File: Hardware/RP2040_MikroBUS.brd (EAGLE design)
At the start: 30.5 x 94 mm, 144 parts, among them J1 SWD, J3 Qwiic, J5 USB C, J6 microSD, Q1 20V/4.2A/52mΩ/1.4W, U2 MAX17048, U3 MCP73831, U4 W25QXX128MBIT, U5 RP2040, U6 WS2812-2020, U7 3.3V, Y2 12MHz

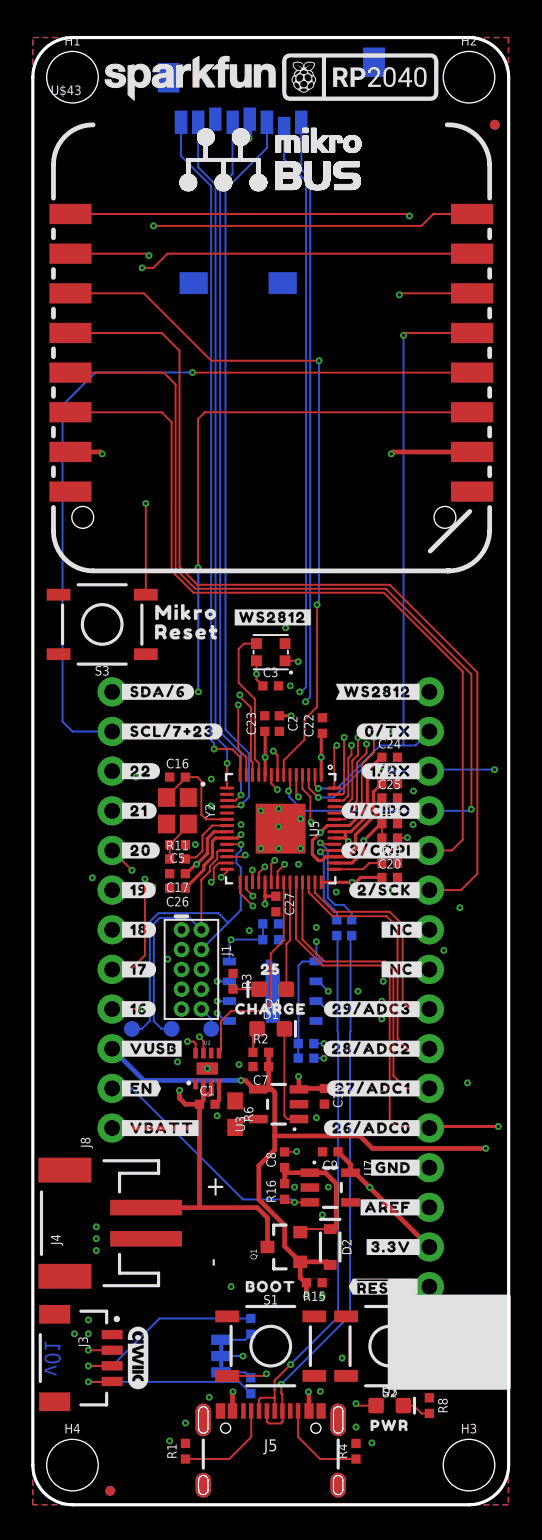
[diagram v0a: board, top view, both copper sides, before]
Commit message: Schematic updates
* Remove values from TPs
* Updated net labels with "!" for active low signals - !BOOT!, !SPI0_CS!, !QSPI-CS!, !BATT_ALERT!
* Updated name, value, and shape of mikroBUS socket sch symbol
* Switched out SD card socket for the new one, did NOT connect the detect pin
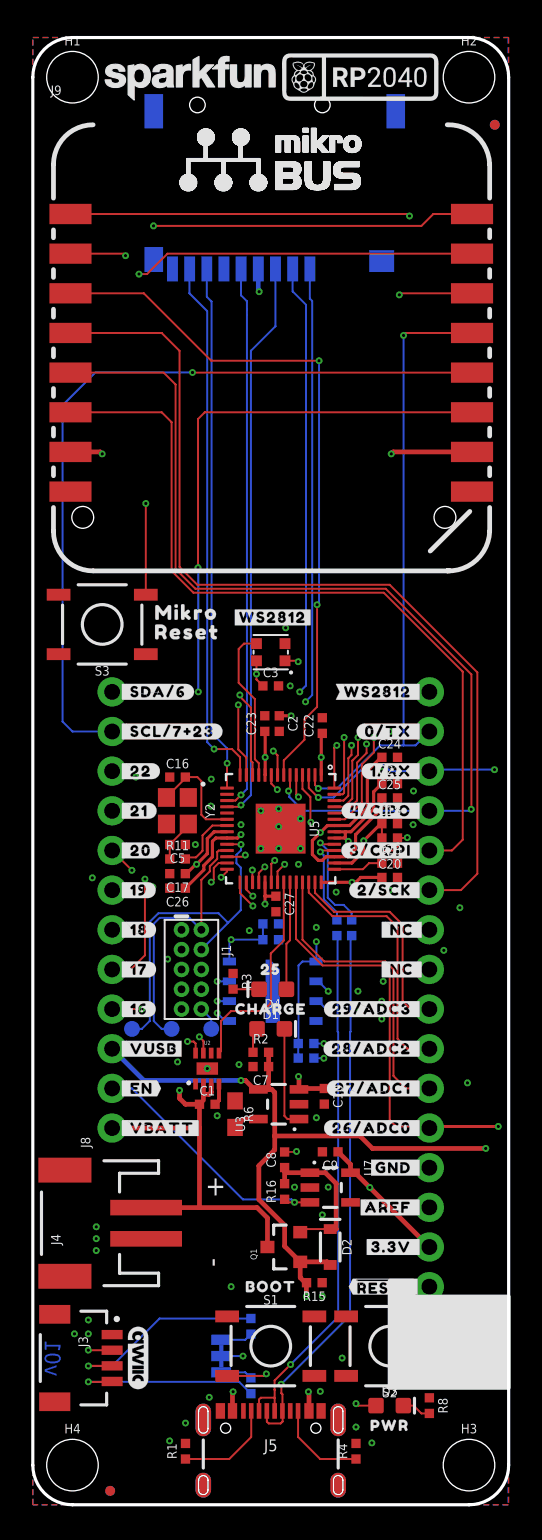
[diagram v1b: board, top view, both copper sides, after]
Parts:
- J6: device SparkFun-Connectors:MICRO-SD-SOCKET -> SparkFun-Connectors:MICROSD-EXTERNALPIN
- moved J6 13.9 mm to (15.5, 89.7), turned to 180 degrees
- renumbered U$43 to J9
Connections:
- net BATT_ALERT renamed !BATT_ALERT!
- net BOOT renamed !BOOT!
- net QSPI-CS renamed !QSPI-CS!
- net SPI0_CS renamed !SPI0_CS!
- net 3.3V: now also J6.4; no longer J6.VCC
- net GND: now also J6.10, J6.11, J6.12, J6.13, J6.6, J6.9; no longer J6.CD1, J6.GND, J6.GND1, J6.GND3
- net SDIO_DAT1: now also J6.8; no longer J6.DAT1
- net SDIO_DAT2: now also J6.1; no longer J6.DAT2
- net SPI_!CS1!/SDIO_DAT3: now also J6.2; no longer J6.CS/DAT3
- net SPI_CIPO1/SDIO_DAT0: now also J6.7; no longer J6.DO/DAT0
- net SPI_COPI1/SDIO_CMD: now also J6.3; no longer J6.DI/CMD
- net SPI_SCK1/SDIO_CLK: now also J6.5; no longer J6.SCLK
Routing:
- net SPI_COPI1/SDIO_CMD: track 46.6 -> 36.2 mm
- net SPI_SCK1/SDIO_CLK: track 45.0 -> 35.1 mm
- net SPI_CIPO1/SDIO_DAT0: track 43.4 -> 33.8 mm
- net SDIO_DAT1: track 44.0 -> 34.4 mm
- net SDIO_DAT2: track 46.6 -> 37.1 mm
- net SPI_!CS1!/SDIO_DAT3: track 46.3 -> 37.0 mm
- net MIK_RST: track 26.9 -> 26.3 mm

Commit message: Board updates
* Fix RESET button label
* Add RP2040 to SF microcontroller library and update in sch/board
* Gave some more space between the new traces I placed
* Brought D+ and D- traces closer together
* Changed "WS2812" label to text only
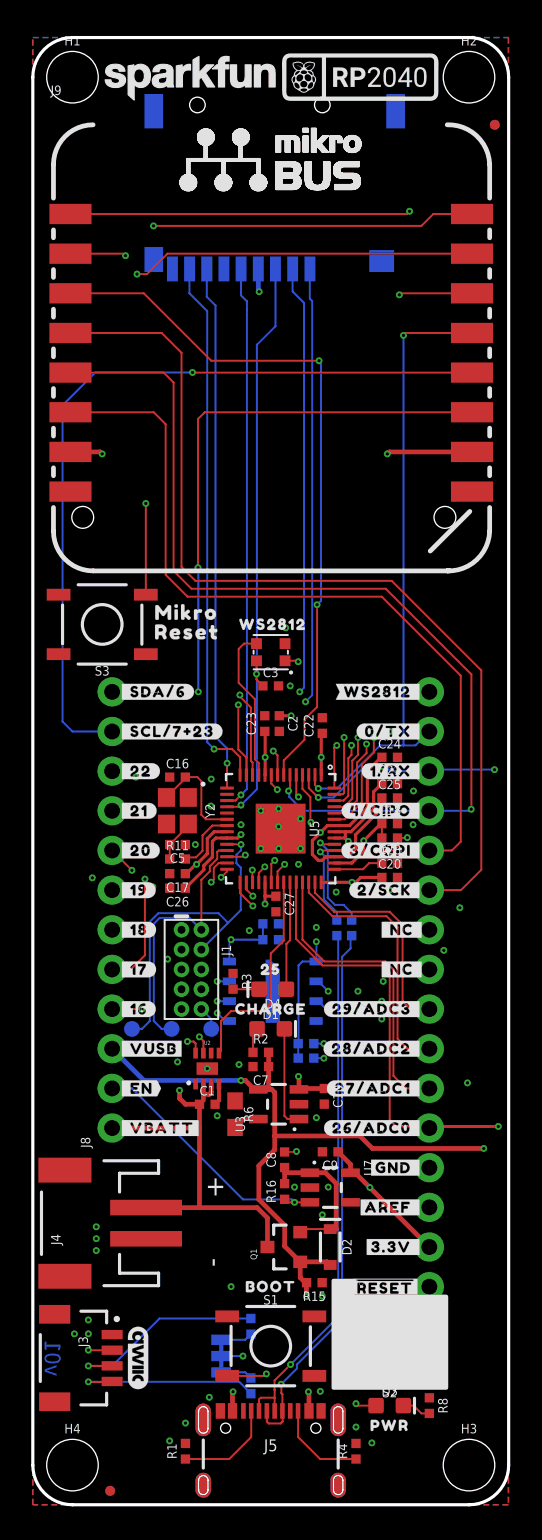
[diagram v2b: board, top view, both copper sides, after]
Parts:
- removed U$60: (no value), output:#WS2812#0
- added U$30: (no value), output:WS28120
- U5: device RP2040:QFN-56 -> SparkFun-IC-Microcontroller:QFN-56
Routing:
- net I2C1_SCL/GPIO23: track 140.4 -> 139.2 mm

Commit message: Run checklist
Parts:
- removed U$45: (no value), SparkFun-Aesthetics:SFE_LOGO_NAME_.1
- added LOGO1: OSHW-LOGOS, SparkFun-Aesthetics:OSHW-LOGO-S
- added LOGO2: SFE_LOGO_NAME.1_INCH, SparkFun-Aesthetics:SFE_LOGO_NAME_.1
- D5: value WS2812-2020 -> WS2812_2020
- renumbered JP1 to I2C, U6 to D5
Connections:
- net 3.3V: now also D5.VCC; no longer D5.4
- net GND: now also D5.GND; no longer D5.2
- net WS2812_DI: now also D5.DI; no longer D5.3
- net WS2812_DO: now also D5.DO; no longer D5.1
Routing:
- net SPI_!CS1!/SDIO_DAT3: track 36.9 -> 38.7 mm
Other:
- board text added: "1"
- board text added: "2"
- board text added: "3"
- board text added: "4"
- board text added: "Revised by: Priyanka Makin"

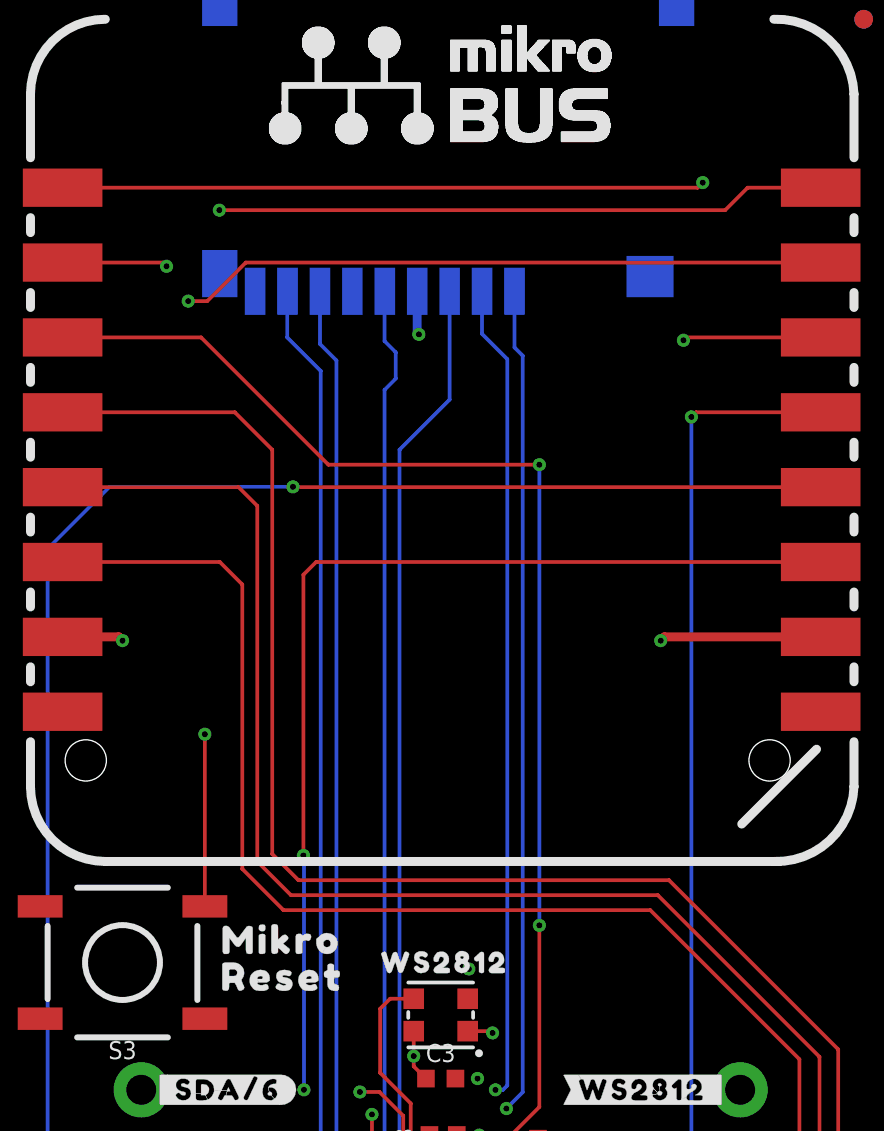
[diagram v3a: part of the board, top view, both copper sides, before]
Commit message: MikroE updates
* Change button label from "Mik Reset" to "Mikroe Reset"
* Added mikroBUS pin names
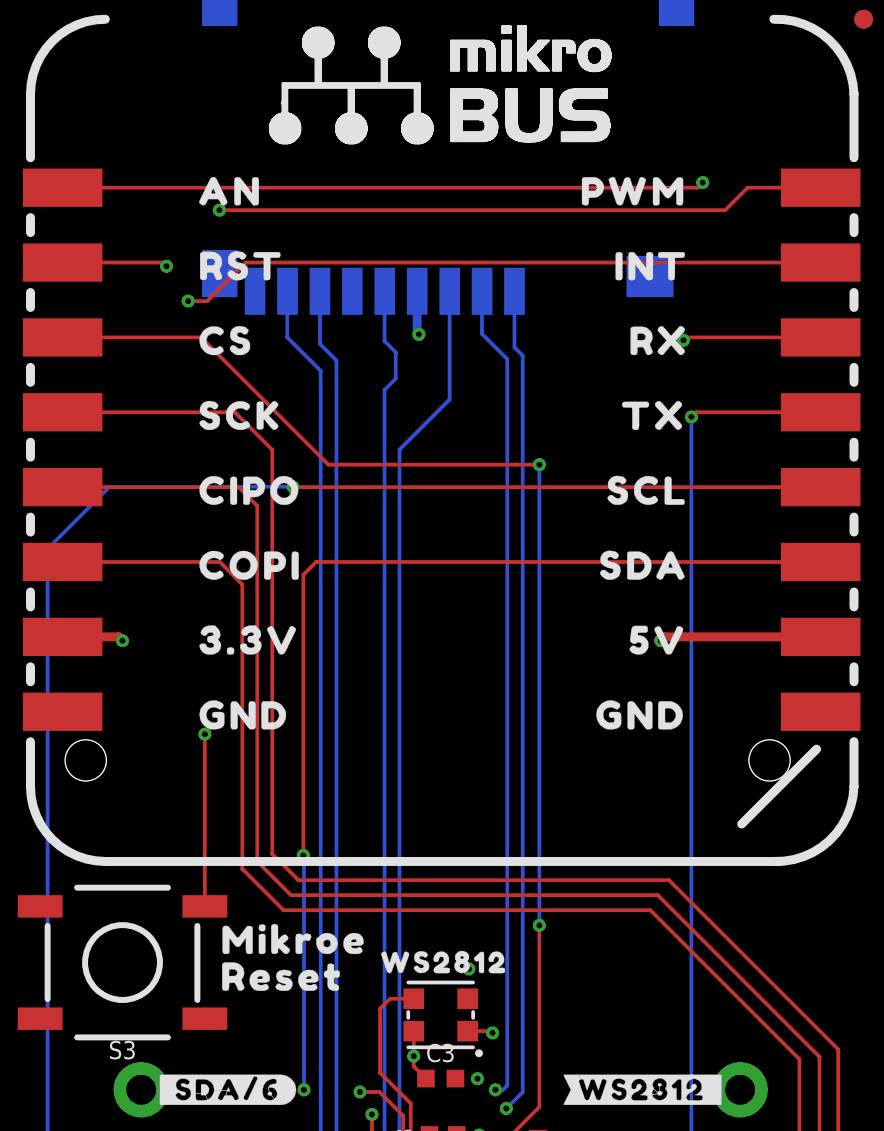
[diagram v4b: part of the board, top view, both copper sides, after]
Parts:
- added U$43: (no value), output:MIKROE0
- added U$44: (no value), output:RST0
- added U$45: (no value), output:CS0
- added U$60: (no value), output:CIPO0
- added U$74: (no value), output:SCK0
- added U$75: (no value), output:COPI0
- added U$76: (no value), output:3#3V0
- added U$77, U$78: (no value), output:GND0
- added U$79: (no value), output:5V0
- added U$80: (no value), output:SDA0
- added U$81: (no value), output:SCL0
- added U$82: (no value), output:TX0
- added U$83: (no value), output:RX0
- added U$84: (no value), output:INT0
- added U$85: (no value), output:PWM0
- U$29: device output:MIKRO0 -> output:AN0
- moved U$29 25.4 mm to (6.35, 82.5)
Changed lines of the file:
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@@
 <layer number="37" name="tTest" color="7" fill="1" visible="no" active="yes"/>
 <layer number="38" name="bTest" color="7" fill="1" visible="no" active="yes"/>
-<layer number="39" name="tKeepout" color="4" fill="11" visible="yes" active="yes"/>
+<layer number="39" name="tKeepout" color="4" fill="11" visible="no" active="yes"/>
 <layer number="40" name="bKeepout" color="1" fill="11" visible="no" active="yes"/>
 <layer number="41" name="tRestrict" color="4" fill="10" visible="no" active="yes"/>
@@
 <layer number="45" name="Holes" color="7" fill="1" visible="yes" active="yes"/>
 <layer number="46" name="Milling" color="3" fill="1" visible="no" active="yes"/>
-<layer number="47" name="Measures" color="7" fill="1" visible="yes" active="yes"/>
+<layer number="47" name="Measures" color="7" fill="1" visible="no" active="yes"/>
 <layer number="48" name="Document" color="7" fill="1" visible="no" active="yes"/>
 <layer number="49" name="Reference" color="7" fill="1" visible="no" active="yes"/>
@@
 <layer number="95" name="Names" color="7" fill="1" visible="no" active="no"/>
 <layer number="96" name="Values" color="7" fill="1" visible="no" active="no"/>
-<layer number="2" name="gndvert" color="10" fill="7" visible="yes" active="yes"/>
-<layer number="15" name="pwrhorz" color="4" fill="7" visible="yes" active="yes"/>
+<layer number="2" name="gndvert" color="10" fill="7" visible="no" active="yes"/>
+<layer number="15" name="pwrhorz" color="4" fill="7" visible="no" active="yes"/>
 <layer number="3" name="Route3" color="4" fill="3" visible="no" active="no"/>
 <layer number="4" name="Route4" color="1" fill="4" visible="no" active="no"/>
@@
 <element name="U$17" library="SparkFun-Aesthetics" package="RASPI_RP2040_LOGO_10MM" value="RASPI_RP2040_LOGO_10MM" x="12.7" y="15.24" smashed="yes" rot="MR0"/>
 <element name="U$73" library="SparkFun-Aesthetics" package="RASPI_RP2040_LOGO_10MM" value="RASPI_RP2040_LOGO_10MM" x="20.955" y="91.44" smashed="yes"/>
-<element name="U$29" library="output" package="MIKRO0" value="" x="7.112" y="57.15" smashed="yes"/>
 <element name="U$30" library="output" package="WS28120" value="" x="12.7" y="56.388" smashed="yes"/>
 <element name="LOGO1" library="SparkFun-Aesthetics" package="OSHW-LOGO-S" value="OSHW-LOGOS" x="24.003" y="2.032" smashed="yes"/>
@@
 <attribute name="PROD_ID" value="DIO-15591" x="15.24" y="54.61" size="1.778" layer="27" font="vector" ratio="15" display="off"/>
 </element>
+<element name="U$43" library="output" package="MIKROE0" value="" x="7.112" y="57.15" smashed="yes"/>
+<element name="U$29" library="output" package="AN0" value="" x="6.35" y="82.55" smashed="yes"/>
+<element name="U$44" library="output" package="RST0" value="" x="6.35" y="80.01" smashed="yes"/>
+<element name="U$45" library="output" package="CS0" value="" x="6.35" y="77.47" smashed="yes"/>
+<element name="U$60" library="output" package="CIPO0" value="" x="6.35" y="72.39" smashed="yes"/>
+<element name="U$74" library="output" package="SCK0" value="" x="6.35" y="74.93" smashed="yes"/>
+<element name="U$75" library="output" package="COPI0" value="" x="6.35" y="69.85" smashed="yes"/>
+<element name="U$76" library="output" package="3#3V0" value="" x="6.35" y="67.31" smashed="yes"/>
+<element name="U$77" library="output" package="GND0" value="" x="6.35" y="64.77" smashed="yes"/>
+<element name="U$78" library="output" package="GND0" value="" x="19.812" y="64.77" smashed="yes"/>
+<element name="U$79" library="output" package="5V0" value="" x="20.955" y="67.31" smashed="yes"/>
+<element name="U$80" library="output" package="SDA0" value="" x="19.939" y="69.85" smashed="yes"/>
+<element name="U$81" library="output" package="SCL0" value="" x="20.193" y="72.39" smashed="yes"/>
+<element name="U$82" library="output" package="TX0" value="" x="20.701" y="74.93" smashed="yes"/>
+<element name="U$83" library="output" package="RX0" value="" x="20.955" y="77.47" smashed="yes"/>
+<element name="U$84" library="output" package="INT0" value="" x="20.447" y="80.01" smashed="yes"/>
+<element name="U$85" library="output" package="PWM0" value="" x="19.304" y="82.55" smashed="yes"/>
 </elements>
 <signals>
